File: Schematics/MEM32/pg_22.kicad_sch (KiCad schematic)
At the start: 7 parts, among them U1806 XLRULOGIC, U1901 F244, U1903 TSXXPAL, U1905 MUXLPAL, U1907 F258, U1908 F258, U2908 F64

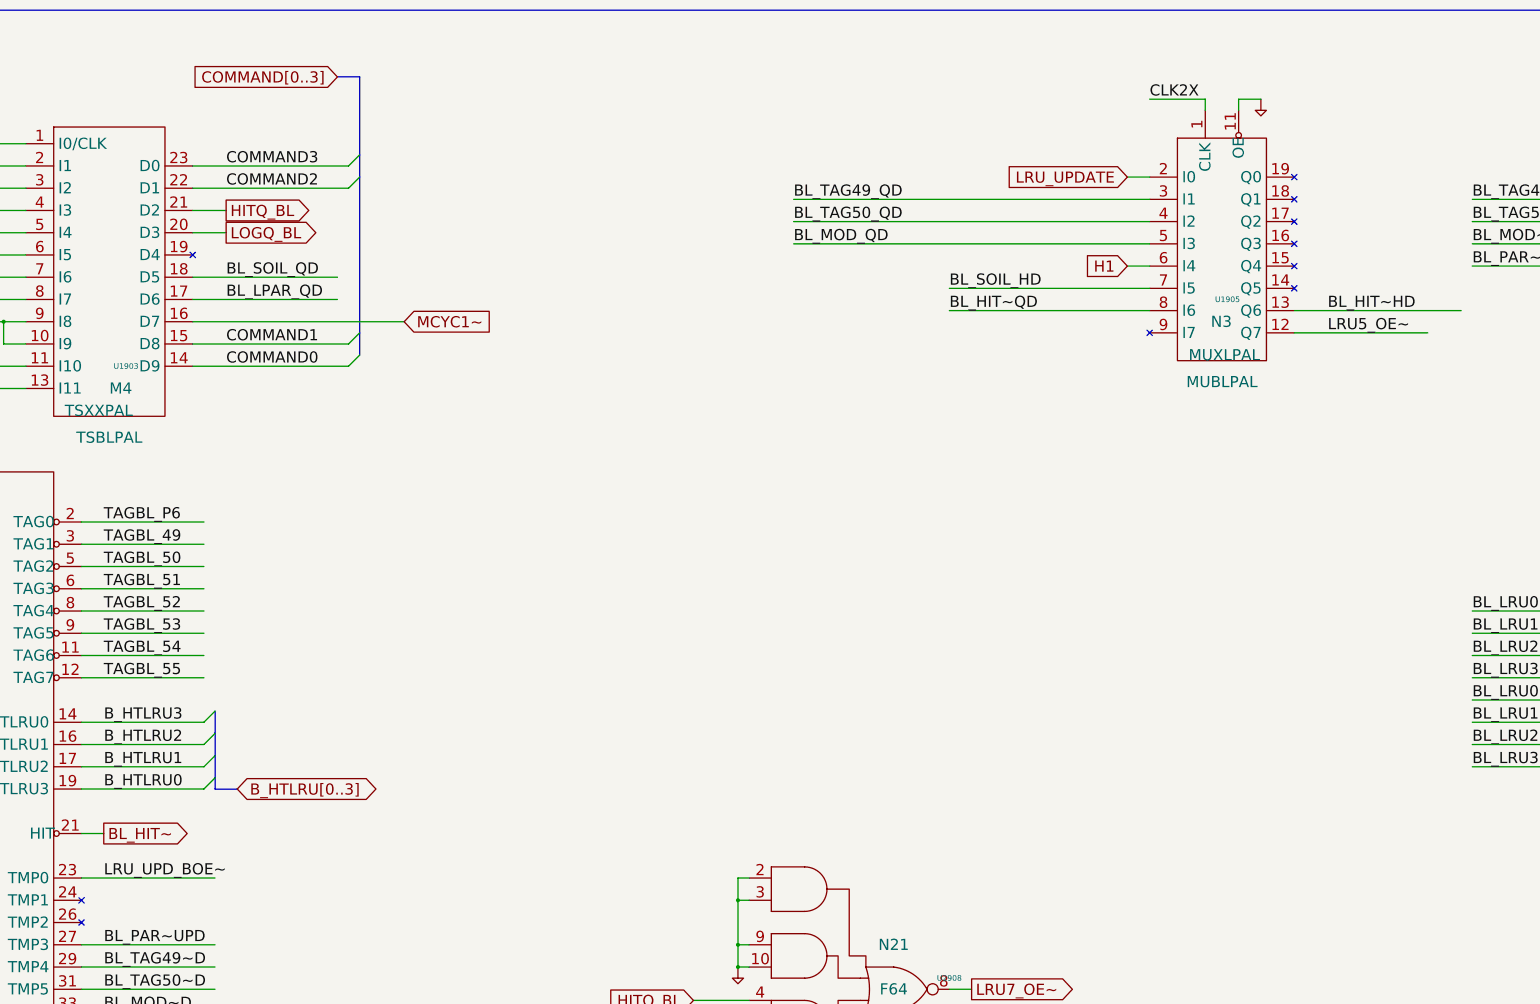
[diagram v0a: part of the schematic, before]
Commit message: MEM32: eliminate MUBLPAL, tested to 16.15 (rm120)
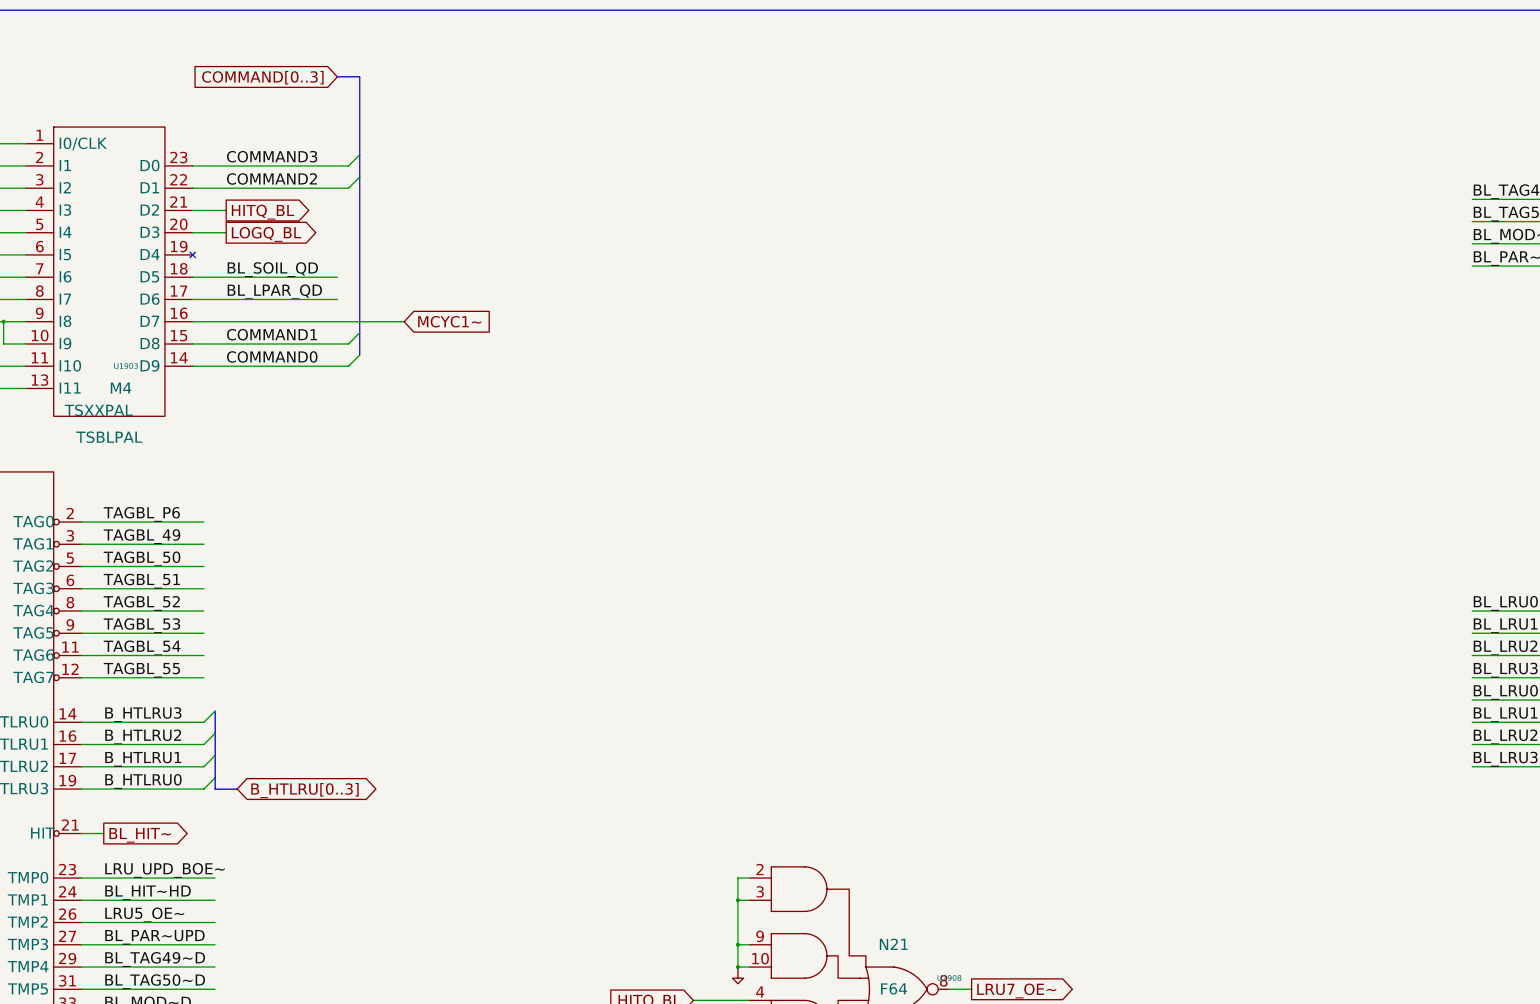
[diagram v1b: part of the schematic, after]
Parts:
- removed U1905: MUXLPAL, symbol r1000:MUXLPAL
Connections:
- net BL_HIT~HD: now also U1806.24 (TMP1)
- net LRU5_OE~: now also U1806.26 (TMP2)
- no-connect marks 16 -> 7
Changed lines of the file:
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@@
   (no_connect (at 152.4 71.12))
   (no_connect (at 66.04 259.08))
-  (no_connect (at 370.84 88.9))
   (no_connect (at 127 314.96))
-  (no_connect (at 127 223.52))
   (no_connect (at 508 137.16))
-  (no_connect (at 403.86 73.66))
   (no_connect (at 508 43.18))
-  (no_connect (at 403.86 78.74))
-  (no_connect (at 403.86 68.58))
-  (no_connect (at 403.86 58.42))
-  (no_connect (at 127 218.44))
-  (no_connect (at 403.86 53.34))
   (no_connect (at 127 289.56))
   (no_connect (at 279.4 246.38))
-  (no_connect (at 403.86 63.5))
   (bus_entry (at 68.58 63.5) (size 2.54 2.54)
     (stroke (width 0) (type default))
@@
     (stroke (width 0) (type default))
   )
-  (wire (pts (xy 383.54 35.56) (xy 383.54 38.1))
-    (stroke (width 0) (type default))
-  )
   (wire (pts (xy 515.62 30.48) (xy 515.62 43.18))
     (stroke (width 0) (type default))
@@
     (stroke (width 0) (type default))
   )
-  (wire (pts (xy 365.76 73.66) (xy 370.84 73.66))
-    (stroke (width 0) (type default))
-  )
   (bus (pts (xy 68.58 63.5) (xy 68.58 68.58))
     (stroke (width 0) (type default))
@@
     (stroke (width 0) (type default))
   )
-  (wire (pts (xy 370.84 58.42) (xy 289.56 58.42))
-    (stroke (width 0) (type default))
-  )
   (wire (pts (xy 487.68 58.42) (xy 487.68 78.74))
     (stroke (width 0) (type default))
@@
     (stroke (width 0) (type default))
   )
-  (wire (pts (xy 370.84 68.58) (xy 289.56 68.58))
-    (stroke (width 0) (type default))
-  )
   (bus (pts (xy 190.5 48.26) (xy 190.5 53.34))
     (stroke (width 0) (type default))
@@
     (stroke (width 0) (type default))
   )
-  (wire (pts (xy 289.56 63.5) (xy 370.84 63.5))
-    (stroke (width 0) (type default))
-  )
   (wire (pts (xy 66.04 55.88) (xy 114.3 55.88))
     (stroke (width 0) (type default))
@@
     (stroke (width 0) (type default))
   )
-  (wire (pts (xy 365.76 53.34) (xy 370.84 53.34))
-    (stroke (width 0) (type default))
-  )
   (wire (pts (xy 200.66 86.36) (xy 152.4 86.36))
     (stroke (width 0) (type default))
@@
     (stroke (width 0) (type default))
   )
-  (wire (pts (xy 391.16 35.56) (xy 396.24 35.56))
-    (stroke (width 0) (type default))
-  )
   (wire (pts (xy 45.72 111.76) (xy 50.8 111.76))
     (stroke (width 0) (type default))
@@
     (stroke (width 0) (type default))
   )
+  (wire (pts (xy 127 223.52) (xy 157.48 223.52))
+    (stroke (width 0) (type default))
+  )
   (wire (pts (xy 495.3 78.74) (xy 487.68 78.74))
     (stroke (width 0) (type default))
@@
     (stroke (width 0) (type default))
   )
+  (wire (pts (xy 127 218.44) (xy 157.48 218.44))
+    (stroke (width 0) (type default))
+  )
   (wire (pts (xy 276.86 218.44) (xy 276.86 228.6))
     (stroke (width 0) (type default))
@@
     (stroke (width 0) (type default))
   )
-  (wire (pts (xy 391.16 35.56) (xy 391.16 38.1))
-    (stroke (width 0) (type default))
-  )
-  (wire (pts (xy 325.12 78.74) (xy 370.84 78.74))
-    (stroke (width 0) (type default))
-  )
   (wire (pts (xy 297.18 320.04) (xy 302.26 320.04))
     (stroke (width 0) (type default))
@@
     (stroke (width 0) (type default))
   )
-  (wire (pts (xy 403.86 88.9) (xy 434.34 88.9))
-    (stroke (width 0) (type default))
-  )
   (wire (pts (xy 127 279.4) (xy 157.48 279.4))
     (stroke (width 0) (type default))
@@
     (stroke (width 0) (type default))
   )
-  (wire (pts (xy 325.12 83.82) (xy 370.84 83.82))
-    (stroke (width 0) (type default))
-  )
   (bus (pts (xy 347.98 355.6) (xy 353.06 355.6))
     (stroke (width 0) (type default))
@@
     (stroke (width 0) (type default))
   )
-  (wire (pts (xy 403.86 83.82) (xy 441.96 83.82))
-    (stroke (width 0) (type default))
-  )
   (wire (pts (xy 276.86 228.6) (xy 279.4 228.6))
     (stroke (width 0) (type default))
@@
     (stroke (width 0) (type default))
   )
-  (wire (pts (xy 370.84 35.56) (xy 383.54 35.56))
-    (stroke (width 0) (type default))
-  )
   (wire (pts (xy 444.5 63.5) (xy 482.6 63.5))
     (stroke (width 0) (type default))
@@
     (effects (font (size 2.54 2.54)) (justify left bottom))
   )
-  (label "BL_HIT~HD" (at 411.48 83.82 0) (fields_autoplaced)
+  (label "BL_HIT~HD" (at 132.08 218.44 0) (fields_autoplaced)
     (effects (font (size 2.54 2.54)) (justify left bottom))
   )
@@
     (effects (font (size 2.54 2.54)) (justify left bottom))
   )
-  (label "BL_TAG50_QD" (at 289.56 63.5 0) (fields_autoplaced)
-    (effects (font (size 2.54 2.54)) (justify left bottom))
-  )
   (label "BL_LRU3_HD" (at 233.68 340.36 0) (fields_autoplaced)
     (effects (font (size 2.54 2.54)) (justify left bottom))
@@
     (effects (font (size 2.54 2.54)) (justify left bottom))
   )
-  (label "LRU5_OE~" (at 411.48 88.9 0) (fields_autoplaced)
+  (label "LRU5_OE~" (at 132.08 223.52 0) (fields_autoplaced)
     (effects (font (size 2.54 2.54)) (justify left bottom))
   )
@@
     (effects (font (size 2.54 2.54)) (justify left bottom))
   )
-  (label "CLK2X" (at 370.84 35.56 0) (fields_autoplaced)
-    (effects (font (size 2.54 2.54)) (justify left bottom))
-  )
   (label "TAGBL_50" (at 543.56 71.12 0) (fields_autoplaced)
     (effects (font (size 2.54 2.54)) (justify left bottom))
@@
     (effects (font (size 2.54 2.54)) (justify left bottom))
   )
-  (label "BL_TAG49_QD" (at 289.56 58.42 0) (fields_autoplaced)
-    (effects (font (size 2.54 2.54)) (justify left bottom))
-  )
-  (label "BL_SOIL_HD" (at 325.12 78.74 0) (fields_autoplaced)
-    (effects (font (size 2.54 2.54)) (justify left bottom))
-  )
   (label "BL_LRU0~UPD" (at 444.5 172.72 0) (fields_autoplaced)
     (effects (font (size 2.54 2.54)) (justify left bottom))
@@
     (effects (font (size 2.54 2.54)) (justify left bottom))
   )
-  (label "BL_HIT~QD" (at 325.12 83.82 0) (fields_autoplaced)
-    (effects (font (size 2.54 2.54)) (justify left bottom))
-  )
   (label "CLK2X" (at 93.98 45.72 0) (fields_autoplaced)
     (effects (font (size 2.54 2.54)) (justify left bottom))
@@
   )
   (label "BL_LRU1~UPD" (at 444.5 177.8 0) (fields_autoplaced)
-    (effects (font (size 2.54 2.54)) (justify left bottom))
-  )
-  (label "BL_MOD_QD" (at 289.56 68.58 0) (fields_autoplaced)
     (effects (font (size 2.54 2.54)) (justify left bottom))
   )
@@
     )
   )
-  (global_label "H1" (shape input) (at 365.76 73.66 180) (fields_autoplaced)
-    (effects (font (size 2.54 2.54)) (justify right))
-    (property "Intersheet References" "${INTERSHEET_REFS}" (at 355.854 73.5013 0)
-      (effects (font (size 1.905 1.905)) (justify right))
-    )
-  )
   (global_label "PHIT_BL~" (shape input) (at 104.14 86.36 180) (fields_autoplaced)
     (effects (font (size 2.54 2.54)) (justify right))
@@
     (property "Intersheet References" "${INTERSHEET_REFS}" (at 45.2483 55.7213 0)
       (effects (font (size 1.905 1.905)) (justify right))
-    )
-  )
-  (global_label "LRU_UPDATE" (shape input) (at 365.76 53.34 180) (fields_autoplaced)
-    (effects (font (size 2.54 2.54)) (justify right))
-    (property "Intersheet References" "${INTERSHEET_REFS}" (at 337.5902 53.1813 0)
-      (effects (font (size 1.905 1.905)) (justify right))
-    )
-  )
-  (symbol (lib_id "r1000:MUXLPAL") (at 386.08 86.36 0) (unit 1)
-    (in_bom yes) (on_board yes) (dnp no)
-    (property "Reference" "U1905" (at 388.62 81.28 0)
-      (effects (font (size 1.27 1.27)))
-    )
-    (property "Value" "MUXLPAL" (at 379.73 93.98 0)
-      (effects (font (size 2.54 2.54)) (justify left))
-    )
-    (property "Footprint" "" (at 387.35 87.63 0)
-      (effects (font (size 1.27 1.27)) hide)
-    )
-    (property "Datasheet" "" (at 387.35 87.63 0)
-      (effects (font (size 1.27 1.27)) hide)
-    )
-    (property "Location" "N3" (at 384.81 86.36 0)
-      (effects (font (size 2.54 2.54)) (justify left))
-    )
-    (property "Name" "MUBLPAL" (at 387.35 101.6 0)
-      (effects (font (size 2.54 2.54)) (justify bottom))
-    )
-    (pin "1")
-    (pin "11")
-    (pin "12")
-    (pin "13")
-    (pin "14")
-    (pin "15")
-    (pin "16")
-    (pin "17")
-    (pin "18")
-    (pin "19")
-    (pin "2")
-    (pin "3")
-    (pin "4")
-    (pin "5")
-    (pin "6")
-    (pin "7")
-    (pin "8")
-    (pin "9")
-    (instances
-      (project "MEM32"
-        (path "/20011966-487c-2cfb-5da0-3540af989df7/20011966-17c5-2cec-227c-0232bf6aae8a"
-          (reference "U1905") (unit 1) (value "MUXLPAL") (footprint "")
-        )
-      )
     )
   )
@@
         )
       )
-    )
-  )
-  (symbol (lib_id "r1000:PD") (at 396.24 35.56 0) (unit 1)
-    (in_bom no) (on_board yes) (dnp no)
-    (property "Reference" "#PWR0105" (at 396.24 35.56 0)
-      (effects (font (size 1.27 1.27)) hide)
-    )
-    (property "Value" "PD" (at 396.24 35.56 0)
-      (effects (font (size 1.27 1.27)) hide)
-    )
-    (property "Footprint" "" (at 396.24 35.56 0)
-      (effects (font (size 1.27 1.27)) hide)
-    )
-    (property "Datasheet" "" (at 396.24 35.56 0)
-      (effects (font (size 1.27 1.27)) hide)
-    )
-    (pin "1")
-    (instances
-      (project "MEM32"
-        (path "/20011966-487c-2cfb-5da0-3540af989df7/20011966-17c5-2cec-227c-0232bf6aae8a"
-          (reference "#PWR0105") (unit 1) (value "PD") (footprint "")
-        )
-      )
